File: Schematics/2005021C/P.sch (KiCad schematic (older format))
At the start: 2 parts

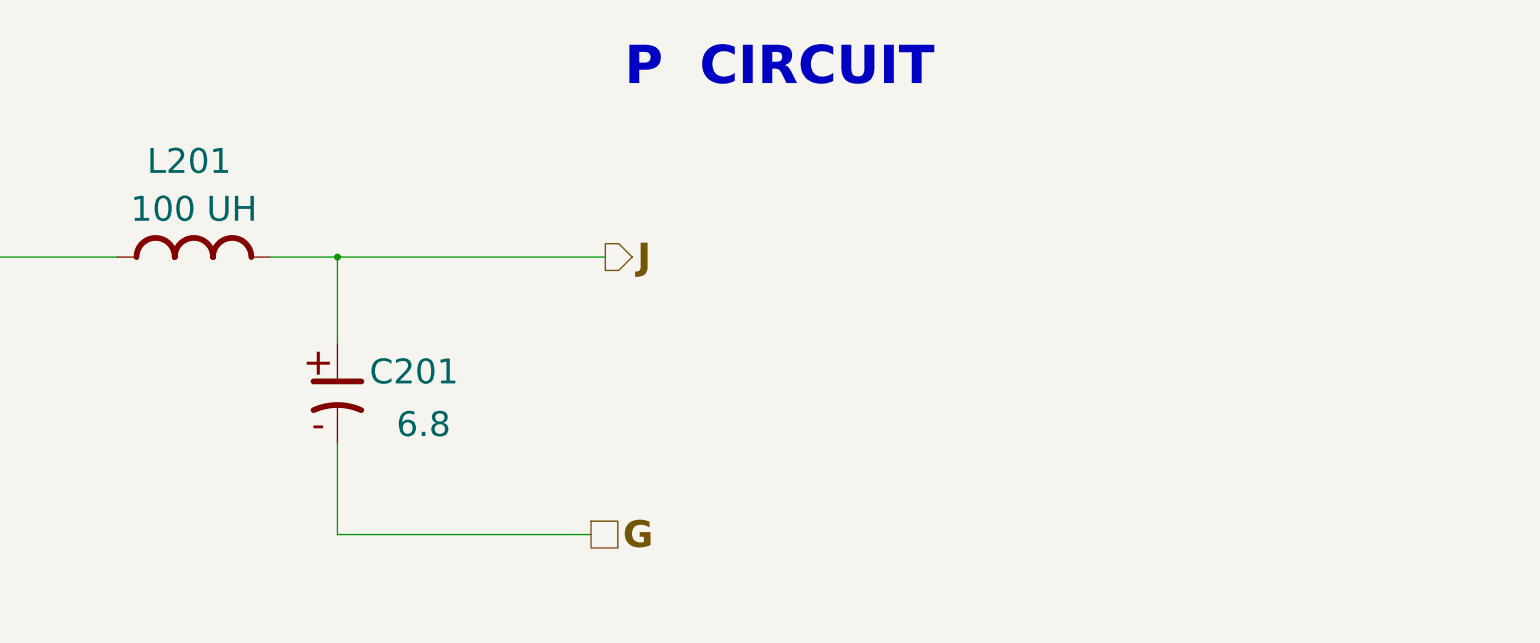
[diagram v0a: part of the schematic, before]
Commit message: Improved the presentation of the CAD for drawing 2005021C somewhat, to correspond a little better to the scan of the original drawing.
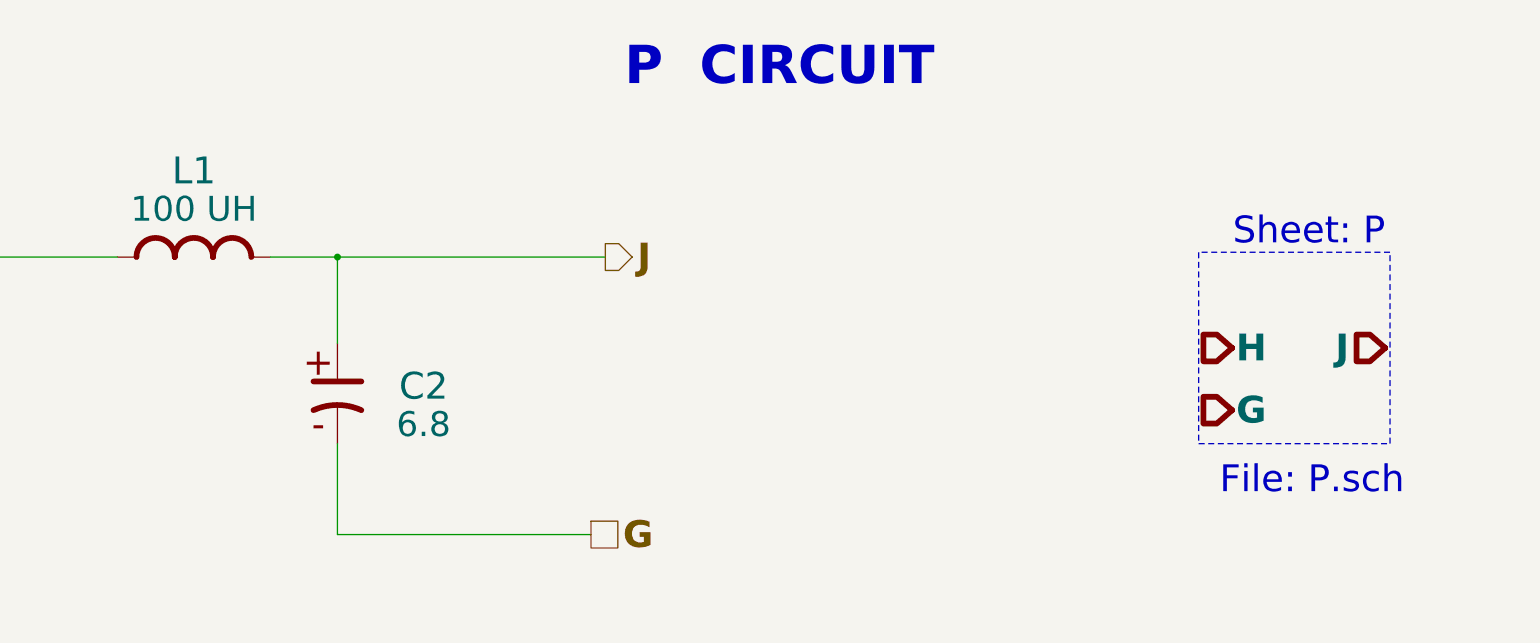
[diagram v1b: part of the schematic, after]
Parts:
- added N201, N202, N203: HierBody, symbol AGC_DSKY:HierBody
- C201: baseRefd (none) -> C2
- L201: baseRefd (none) -> L1
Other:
- note added: "File: P.sch"
- note added: "Sheet: P"
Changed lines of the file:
@@
 $Descr E 44000 34000
 encoding utf-8
-Sheet 16 63
+Sheet 2 63
 Title ""
 Date ""
@@
 AR Path="/5B991709/5CD3D50C" Ref="L1501"  Part="1"
 AR Path="/5B991763/5CD3D50C" Ref="L1601"  Part="1"
-F 0 "L201" H 4500 10975 130 0000 C CNN
+AR Path="/5CD3D50C" Ref="L1"  Part="1"
+F 0 "L201" H 4500 10975 130 0001 C CNN
 F 1 "100 UH" H 4525 10725 130 0000 C CNN
 F 2 "" H 4475 10675 130 0001 C CNN
 F 3 "" H 4475 10675 130 0001 C CNN
+F 4 "L1" H 4525 10925 140 0000 C CNN "baseRefd"
 	1    4525 10475
 	1    0    0    -1
@@
 AR Path="/5B991709/5CD3D5B5" Ref="C1501"  Part="1"
 AR Path="/5B991763/5CD3D5B5" Ref="C1601"  Part="1"
-F 0 "C201" H 5675 11325 130 0000 C CNN
+AR Path="/5CD3D5B5" Ref="C2"  Part="1"
+F 0 "C201" H 5675 11325 130 0001 C CNN
 F 1 "6.8" H 5725 11050 130 0000 C CNN
 F 2 "" H 5275 11600 130 0001 C CNN
 F 3 "" H 5275 11600 130 0001 C CNN
+F 4 "C2" H 5725 11250 140 0000 C CNN "baseRefd"
 	1    5275 11200
 	1    0    0    -1
@@
 Text Notes 6775 9600 0    200  ~ 40
 P  CIRCUIT
+Wire Notes Line style solid
+	9775 11450 10775 11450
+Wire Notes Line style solid
+	10775 11450 10775 10450
+Wire Notes Line style solid
+	10775 10450 9775 10450
+Wire Notes Line style solid
+	9775 10450 9775 11450
+$Comp
+L AGC_DSKY:HierBody N201
+U 1 1 5CF0C9E8
+P 9875 10950
+AR Path="/5B99108F/5CF0C9E8" Ref="N201"  Part="1"
+AR Path="/5B991763/5CF0C9E8" Ref="N1601"  Part="1"
+AR Path="/5B991709/5CF0C9E8" Ref="N1501"  Part="1"
+F 0 "N201" H 9860 10750 140 0001 C CNN
+F 1 "HierBody" H 9880 11130 140 0001 C CNN
+F 2 "" H 9875 10950 140 0001 C CNN
+F 3 "" H 9875 10950 140 0001 C CNN
+F 4 "H" H 10050 10950 140 0000 C CNB "Caption2"
+	1    9875 10950
+	1    0    0    -1
+$EndComp
+$Comp
+L AGC_DSKY:HierBody N202
+U 1 1 5CF0CA10
+P 9875 11275
+AR Path="/5B99108F/5CF0CA10" Ref="N202"  Part="1"
+AR Path="/5B991763/5CF0CA10" Ref="N1602"  Part="1"
+AR Path="/5B991709/5CF0CA10" Ref="N1502"  Part="1"
+F 0 "N202" H 9860 11075 140 0001 C CNN
+F 1 "HierBody" H 9880 11455 140 0001 C CNN
+F 2 "" H 9875 11275 140 0001 C CNN
+F 3 "" H 9875 11275 140 0001 C CNN
+F 4 "G" H 10050 11275 140 0000 C CNB "Caption2"
+	1    9875 11275
+	1    0    0    -1
+$EndComp
+$Comp
+L AGC_DSKY:HierBody N203
+U 1 1 5CF0CA38
+P 10675 10950
+AR Path="/5B99108F/5CF0CA38" Ref="N203"  Part="1"
+AR Path="/5B991763/5CF0CA38" Ref="N1603"  Part="1"
+AR Path="/5B991709/5CF0CA38" Ref="N1503"  Part="1"
+F 0 "N203" H 10660 10750 140 0001 C CNN
+F 1 "HierBody" H 10680 11130 140 0001 C CNN
+F 2 "" H 10675 10950 140 0001 C CNN
+F 3 "" H 10675 10950 140 0001 C CNN
+F 4 "J" H 10525 10950 140 0000 C CNB "Caption2"
+	1    10675 10950
+	1    0    0    -1
+$EndComp
+Text Notes 10850 11725 2    140  ~ 0
+File: P.sch
+Text Notes 10750 10425 2    140  ~ 0
+Sheet: P
 $EndSCHEMATC

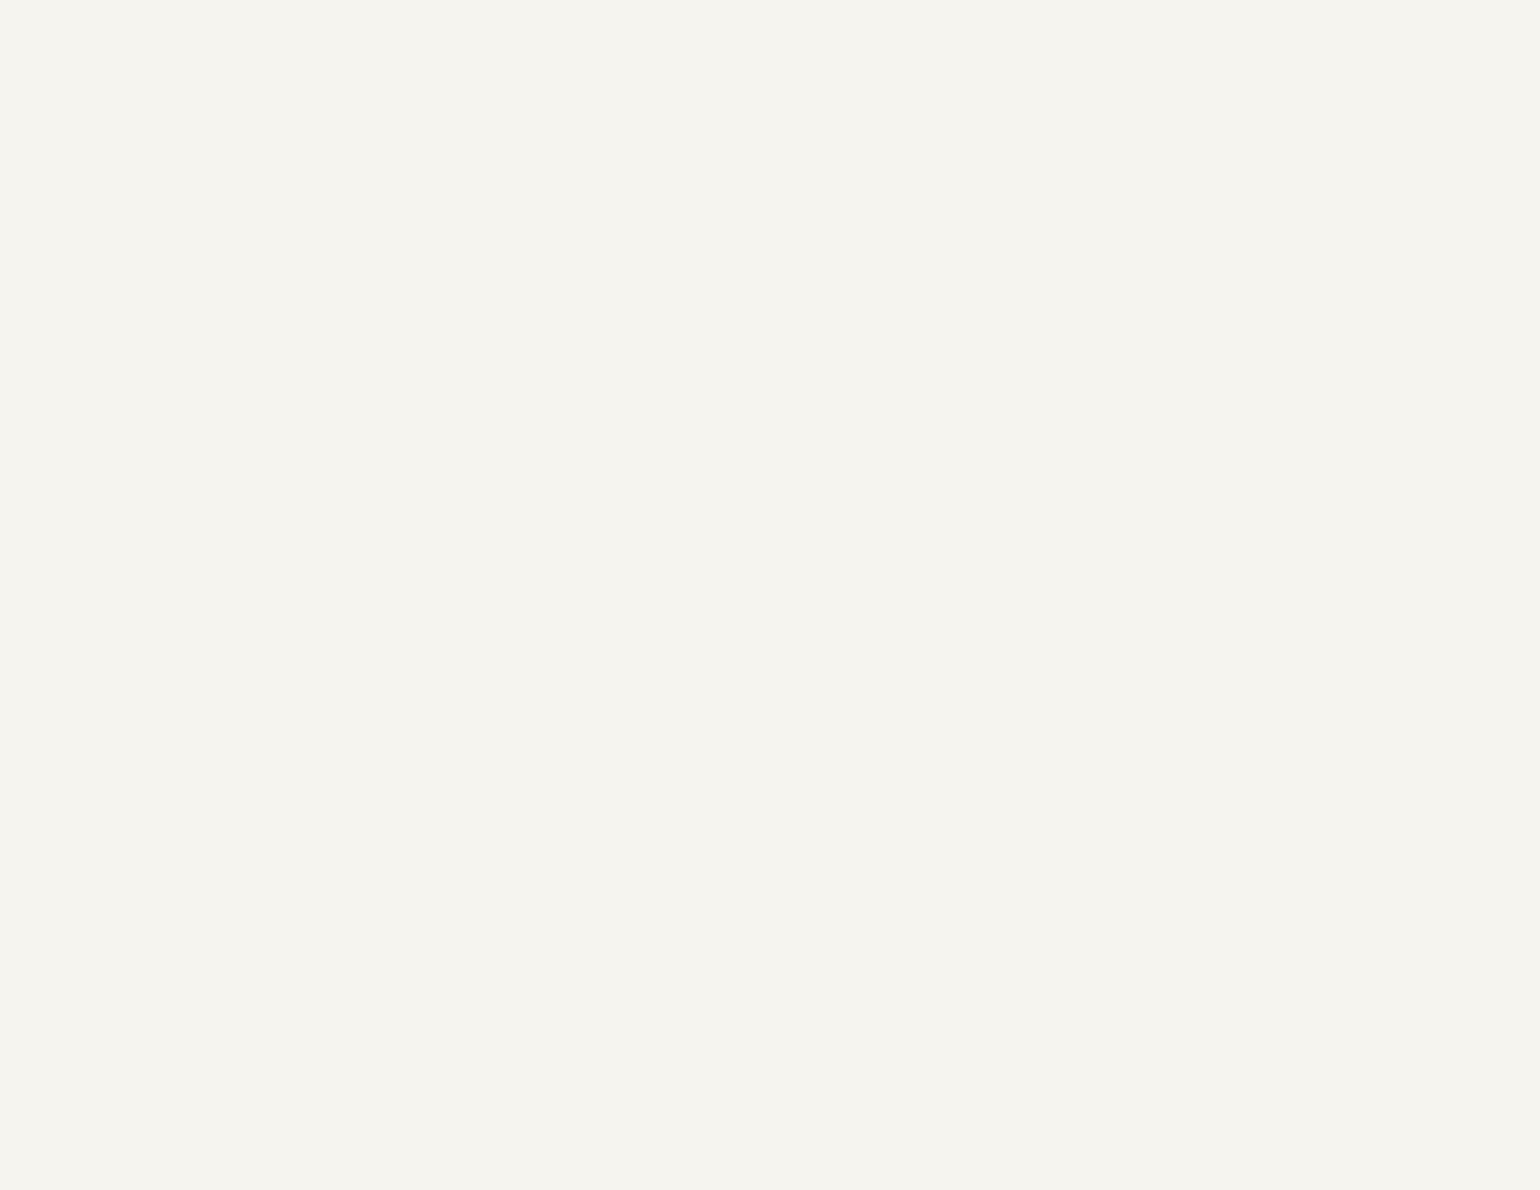
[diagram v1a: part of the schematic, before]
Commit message: Added some improvements to CAD drawing 2005021C ... primarily, moving notes onto more-relevant sheets.
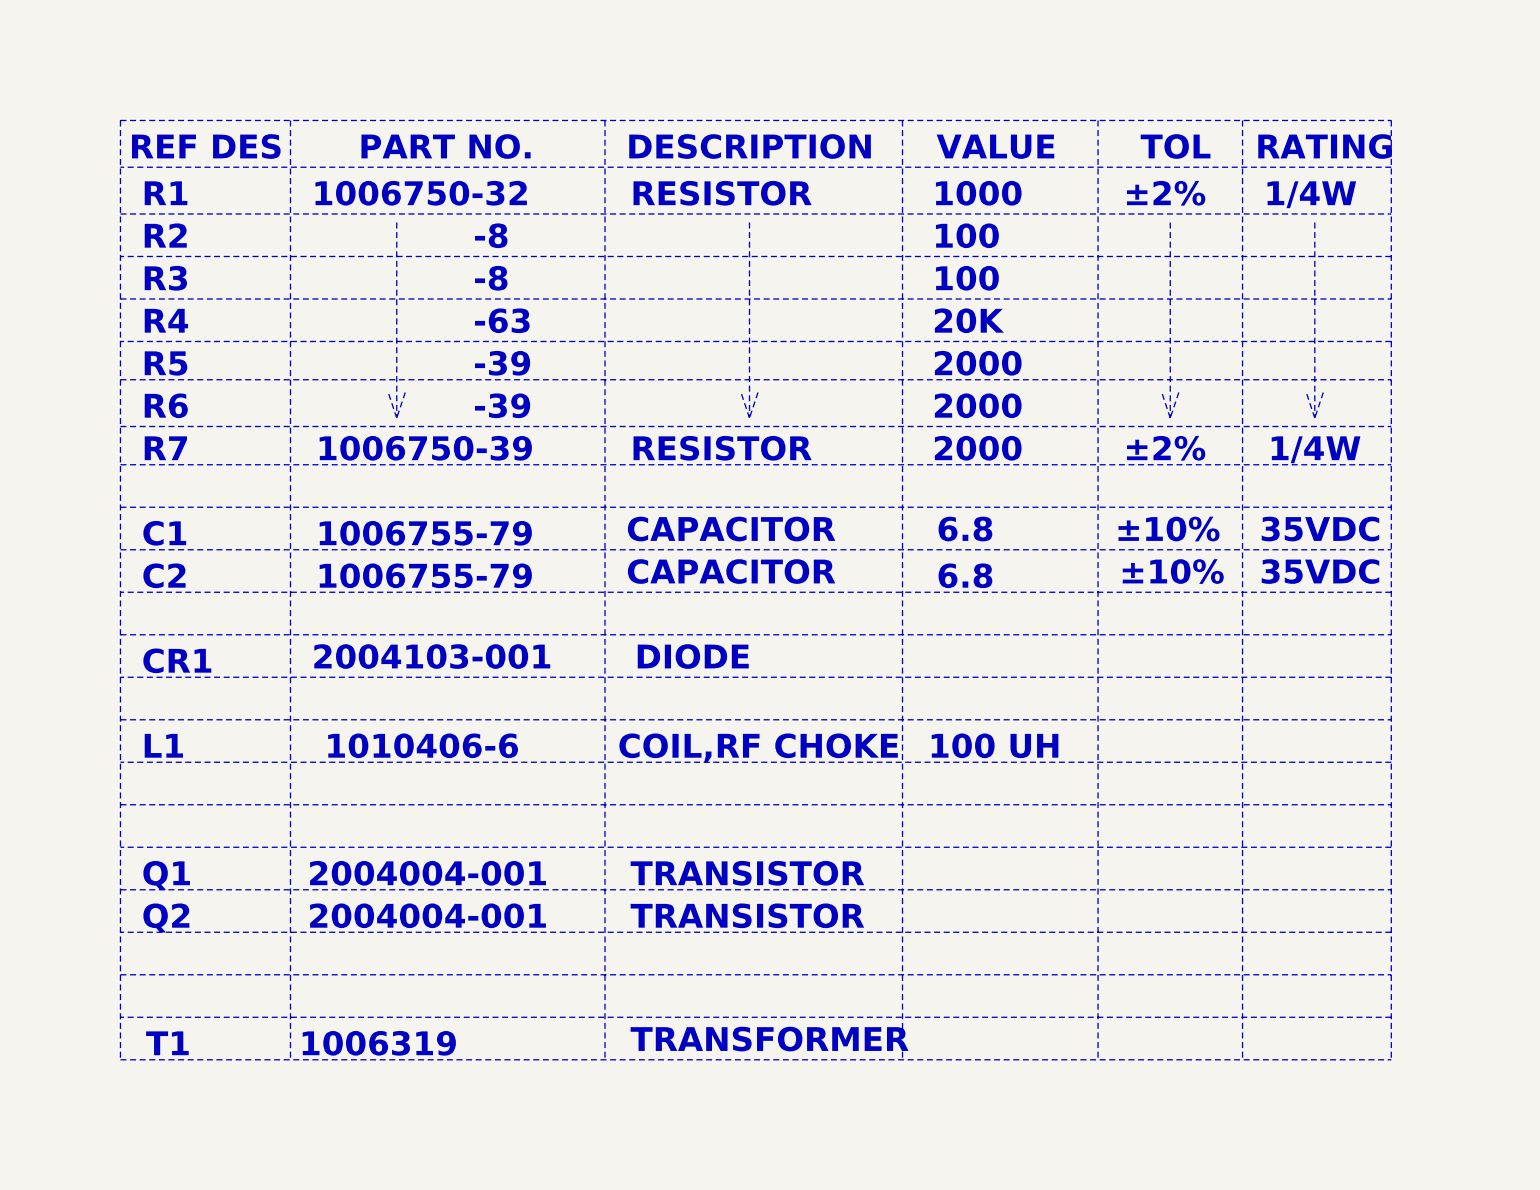
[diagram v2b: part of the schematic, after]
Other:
- note added: "-39"
- note added: "-63"
- note added: "-8"
- note added: "1/4W"
- note added: "100"
- note added: "100 UH"
- note added: "1000"
- note added: "1006319"
- note added: "1006750-32"
- note added: "1006750-39"
- note added: "1006755-79"
- note added: "1010406-6"
- note added: "2000"
- note added: "2004004-001"
- note added: "2004103-001"
- note added: "20K"
- note added: "35VDC"
- note added: "6.8"
- note added: "C1"
- note added: "C2"
- note added: "CAPACITOR"
- note added: "COIL,RF CHOKE"
- note added: "CR1"
- note added: "DESCRIPTION"
- note added: "DIODE"
- note added: "L1"
- note added: "PART NO."
- note added: "Q1"
- note added: "Q2"
- note added: "R1"
- note added: "R2"
- note added: "R3"
- note added: "R4"
- note added: "R5"
- note added: "R6"
- note added: "R7"
- note added: "RATING"
- note added: "REF DES"
- note added: "RESISTOR"
- note added: "T1"
- note added: "TOL"
- note added: "TRANSFORMER"
- note added: "TRANSISTOR"
- note added: "VALUE"
- note added: "±10%"
- note added: "±2%"
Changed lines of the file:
@@
 Text Notes 10750 10425 2    140  ~ 0
 Sheet: P
+Wire Notes Line style solid
+	35526 20780 43001 20780
+Wire Notes Line style solid
+	43001 21055 35526 21055
+Wire Notes Line style solid
+	35526 21330 43001 21330
+Wire Notes Line style solid
+	43001 21580 35526 21580
+Wire Notes Line style solid
+	35526 21830 43001 21830
+Wire Notes Line style solid
+	43001 22080 35526 22080
+Wire Notes Line style solid
+	35526 22305 43001 22305
+Wire Notes Line style solid
+	35526 22580 43001 22580
+Wire Notes Line style solid
+	35526 22805 43001 22805
+Wire Notes Line style solid
+	35526 20780 35526 26305
+Wire Notes Line style solid
+	35526 23055 43001 23055
+Wire Notes Line style solid
+	43001 20780 43001 26305
+Wire Notes Line style solid
+	35526 23305 43001 23305
+Wire Notes Line style solid
+	36526 20780 36526 26305
+Wire Notes Line style solid
+	38376 20780 38376 26305
+Wire Notes Line style solid
+	40126 20780 40126 26305
+Wire Notes Line style solid
+	41276 20780 41276 26305
+Wire Notes Line style solid
+	42126 20780 42126 26305
+Wire Notes Line style solid
+	35526 26305 43001 26305
+Wire Notes Line style solid
+	43001 26055 35526 26055
+Wire Notes Line style solid
+	35526 25805 43001 25805
+Wire Notes Line style solid
+	43001 25555 35526 25555
+Wire Notes Line style solid
+	35526 25305 43001 25305
+Wire Notes Line style solid
+	43001 25055 35526 25055
+Wire Notes Line style solid
+	35526 24805 43001 24805
+Wire Notes Line style solid
+	43001 24555 35526 24555
+Wire Notes Line style solid
+	35526 24305 43001 24305
+Wire Notes Line style solid
+	43001 24055 35526 24055
+Wire Notes Line style solid
+	35526 23805 43001 23805
+Wire Notes Line style solid
+	43001 23555 35526 23555
+Text Notes 35576 21030 0    140  ~ 28
+REF DES
+Text Notes 36926 21030 0    140  ~ 28
+PART NO.
+Text Notes 38501 21030 0    140  ~ 28
+DESCRIPTION
+Text Notes 40326 21030 0    140  ~ 28
+VALUE
+Text Notes 41526 21030 0    140  ~ 28
+TOL
+Text Notes 42201 21030 0    140  ~ 28
+RATING
+Text Notes 35651 21305 0    140  ~ 28
+R1
+Text Notes 35651 21555 0    140  ~ 28
+R2
+Text Notes 35651 21805 0    140  ~ 28
+R3
+Text Notes 35651 22055 0    140  ~ 28
+R4
+Text Notes 35651 22305 0    140  ~ 28
+R5
+Text Notes 35651 22555 0    140  ~ 28
+R6
+Text Notes 35651 22805 0    140  ~ 28
+R7
+Text Notes 35651 23305 0    140  ~ 28
+C1
+Text Notes 35651 23555 0    140  ~ 28
+C2
+Text Notes 35651 24055 0    140  ~ 28
+CR1
+Text Notes 35651 24555 0    140  ~ 28
+L1
+Text Notes 35651 25305 0    140  ~ 28
+Q1
+Text Notes 35651 25555 0    140  ~ 28
+Q2
+Text Notes 35676 26305 0    140  ~ 28
+T1
+Text Notes 36651 21305 0    140  ~ 28
+1006750-32
+Text Notes 37601 21555 0    140  ~ 28
+-8
+Text Notes 37601 21805 0    140  ~ 28
+-8
+Text Notes 37601 22055 0    140  ~ 28
+-63
+Text Notes 37601 22305 0    140  ~ 28
+-39
+Text Notes 37601 22555 0    140  ~ 28
+-39
+Text Notes 36676 22805 0    140  ~ 28
+1006750-39
+Text Notes 36676 23305 0    140  ~ 28
+1006755-79
+Text Notes 36676 23555 0    140  ~ 28
+1006755-79
+Text Notes 36651 24030 0    140  ~ 28
+2004103-001
+Text Notes 36726 24555 0    140  ~ 28
+1010406-6
+Text Notes 36626 25305 0    140  ~ 28
+2004004-001
+Text Notes 36626 25555 0    140  ~ 28
+2004004-001
+Text Notes 36576 26305 0    140  ~ 28
+1006319
+Text Notes 38526 21305 0    140  ~ 28
+RESISTOR
+Text Notes 38526 22805 0    140  ~ 28
+RESISTOR
+Text Notes 38501 23280 0    140  ~ 28
+CAPACITOR
+Text Notes 38501 23530 0    140  ~ 28
+CAPACITOR
+Text Notes 38551 24030 0    140  ~ 28
+DIODE
+Text Notes 38451 24555 0    140  ~ 28
+COIL,RF CHOKE
+Text Notes 38526 25305 0    140  ~ 28
+TRANSISTOR
+Text Notes 38526 25555 0    140  ~ 28
+TRANSISTOR
+Text Notes 38526 26280 0    140  ~ 28
+TRANSFORMER
+Text Notes 40301 21305 0    140  ~ 28
+1000
+Text Notes 40301 21555 0    140  ~ 28
+100
+Text Notes 40301 21805 0    140  ~ 28
+100
+Text Notes 40301 22055 0    140  ~ 28
+20K
+Text Notes 40301 22305 0    140  ~ 28
+2000
+Text Notes 40301 22555 0    140  ~ 28
+2000
+Text Notes 40301 22805 0    140  ~ 28
+2000
+Text Notes 40326 23280 0    140  ~ 28
+6.8
+Text Notes 40326 23555 0    140  ~ 28
+6.8
+Text Notes 40276 24555 0    140  ~ 28
+100 UH
+Text Notes 41426 21305 0    140  ~ 28
+±2%
+Text Notes 41426 22805 0    140  ~ 28
+±2%
+Text Notes 41376 23280 0    140  ~ 28
+±10%
+Text Notes 41401 23530 0    140  ~ 28
+±10%
+Text Notes 42251 21305 0    140  ~ 28
+1/4W
+Text Notes 42276 22805 0    140  ~ 28
+1/4W
+Text Notes 42226 23280 0    140  ~ 28
+35VDC
+Text Notes 42226 23530 0    140  ~ 28
+35VDC
+Wire Notes Line width 50 style solid
+	37151 21380 37151 22530
+Wire Notes Line width 50 style solid
+	37151 22530 37101 22380
+Wire Notes Line width 50 style solid
+	37201 22380 37151 22530
+Wire Notes Line width 50 style solid
+	39226 21380 39226 22530
+Wire Notes Line width 50 style solid
+	39226 22530 39176 22380
+Wire Notes Line width 50 style solid
+	39276 22380 39226 22530
+Wire Notes Line width 50 style solid
+	41701 21380 41701 22530
+Wire Notes Line width 50 style solid
+	41701 22530 41651 22380
+Wire Notes Line width 50 style solid
+	41751 22380 41701 22530
+Wire Notes Line width 50 style solid
+	42551 21380 42551 22530
+Wire Notes Line width 50 style solid
+	42551 22530 42501 22380
+Wire Notes Line width 50 style solid
+	42601 22380 42551 22530
 $EndSCHEMATC
